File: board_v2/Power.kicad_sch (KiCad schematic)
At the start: 33 parts

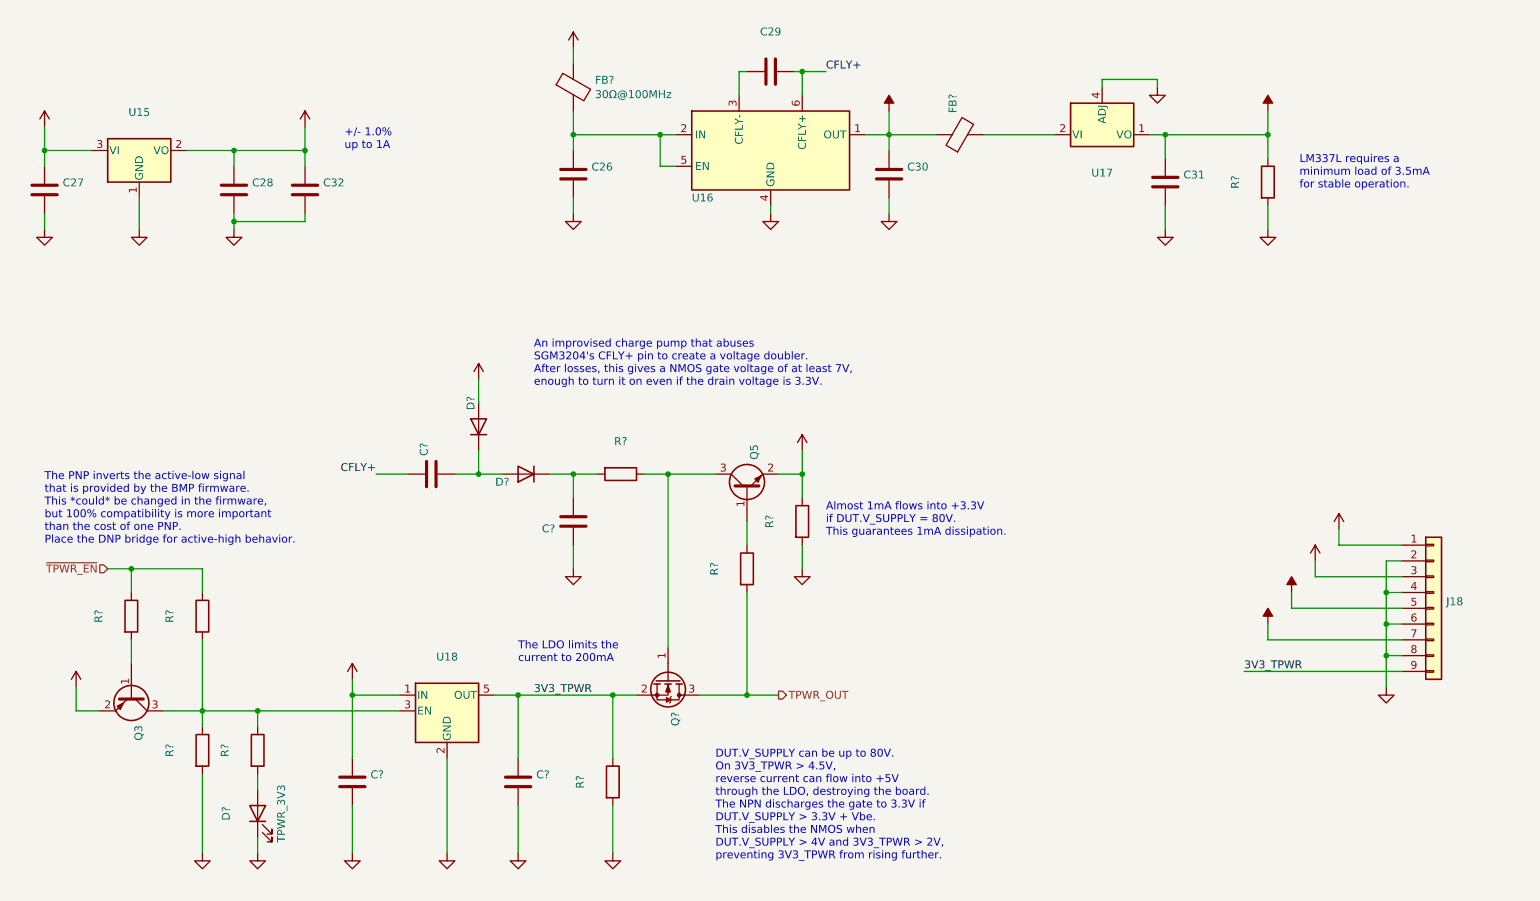
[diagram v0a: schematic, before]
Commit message: Clean up kicad5 files in board_v2
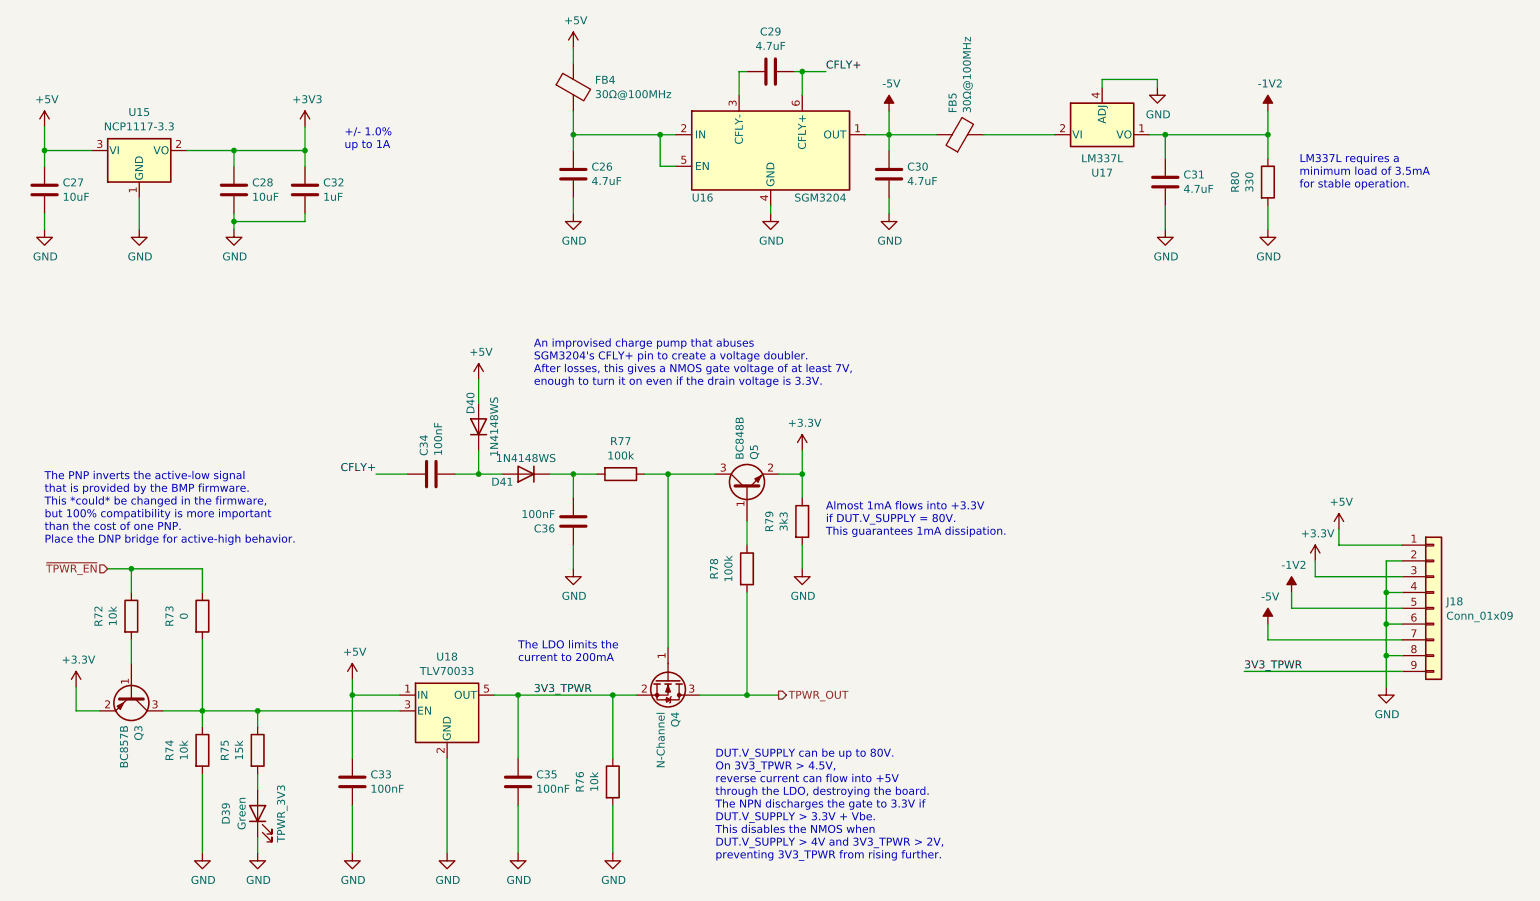
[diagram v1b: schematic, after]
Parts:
- C26, C29, C30, C31: value (none) -> 4.7uF; footprint (none) -> Capacitor_SMD:C_0603_1608Metric_Pad1.05x0.95mm_HandSolder
- C27, C28: value (none) -> 10uF; footprint (none) -> Capacitor_SMD:C_0603_1608Metric_Pad1.05x0.95mm_HandSolder
- C32: value (none) -> 1uF; footprint (none) -> Capacitor_SMD:C_0603_1608Metric_Pad1.05x0.95mm_HandSolder
- C33, C34, C35, C36: renamed from C?; value (none) -> 100nF; footprint (none) -> Capacitor_SMD:C_0603_1608Metric_Pad1.05x0.95mm_HandSolder
- D39: renamed from D?; value (none) -> Green; footprint (none) -> LED_SMD:LED_0805_2012Metric
- D40, D41: renamed from D?; value (none) -> 1N4148WS; footprint (none) -> Diode_SMD:D_SOD-323
- FB5: renamed from FB?; value (none) -> 30Ω@100MHz; footprint (none) -> Resistor_SMD:R_0603_1608Metric_Pad1.05x0.95mm_HandSolder
- J18: value (none) -> Conn_01x09; footprint (none) -> Connector_PinHeader_2.54mm:PinHeader_1x09_P2.54mm_Vertical
- Q3: value (none) -> BC857B; footprint (none) -> Package_TO_SOT_SMD:SOT-23
- Q4: renamed from Q?; value (none) -> N-Channel; footprint (none) -> Package_TO_SOT_SMD:SOT-23
- Q5: value (none) -> BC848B; footprint (none) -> Package_TO_SOT_SMD:SOT-23
- R72, R74, R76: renamed from R?; value (none) -> 10k; footprint (none) -> Resistor_SMD:R_0603_1608Metric_Pad1.05x0.95mm_HandSolder
- R73: renamed from R?; value (none) -> 0; footprint (none) -> Resistor_SMD:R_0603_1608Metric_Pad1.05x0.95mm_HandSolder
- R75: renamed from R?; value (none) -> 15k; footprint (none) -> Resistor_SMD:R_0603_1608Metric_Pad1.05x0.95mm_HandSolder
- R77, R78: renamed from R?; value (none) -> 100k; footprint (none) -> Resistor_SMD:R_0603_1608Metric_Pad1.05x0.95mm_HandSolder
- R79: renamed from R?; value (none) -> 3k3; footprint (none) -> Resistor_SMD:R_0603_1608Metric_Pad1.05x0.95mm_HandSolder
- R80: renamed from R?; value (none) -> 330; footprint (none) -> Resistor_SMD:R_0603_1608Metric_Pad1.05x0.95mm_HandSolder
- U15: value (none) -> NCP1117-3.3; footprint (none) -> Package_TO_SOT_SMD:SOT-223-3_TabPin2
- U16: value (none) -> SGM3204; footprint (none) -> Package_TO_SOT_SMD:SOT-23-6_Handsoldering
- U17: value (none) -> LM337L; footprint (none) -> Package_SO:SOIC-8_3.9x4.9mm_P1.27mm; symbol board-rescue:LM337L_SO8-Regulator_Linear -> Regulator_Linear:LM337L_SO8
- U18: value (none) -> TLV70033; footprint (none) -> Package_TO_SOT_SMD:SOT-23-5_HandSoldering
- gave numbers to parts that had none: 1
